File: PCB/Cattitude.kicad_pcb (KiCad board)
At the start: 2 copper layers, 35 x 25 mm, 14 parts, among them J1 Conn_01x08_Pin, J2 Conn_01x04_Pin, J3 Conn_01x02_Pin, J4 Conn_01x02_Pin, J5 Conn_01x03_Pin, J6 Conn_01x03_Pin, J7 Conn_01x03_Pin, J8 Conn_01x03_Pin, SW2 SW_SPDT, U1 102010551

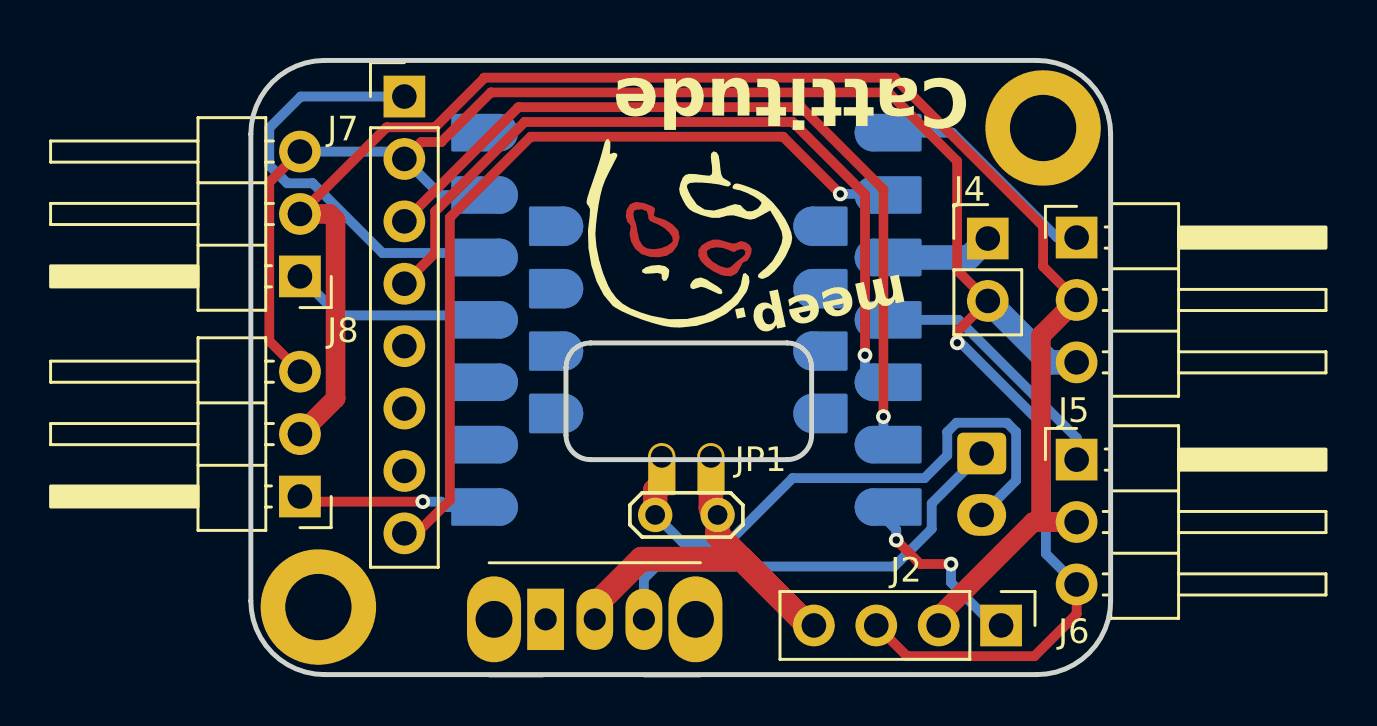
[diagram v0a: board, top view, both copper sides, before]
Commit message: Added GND Pour
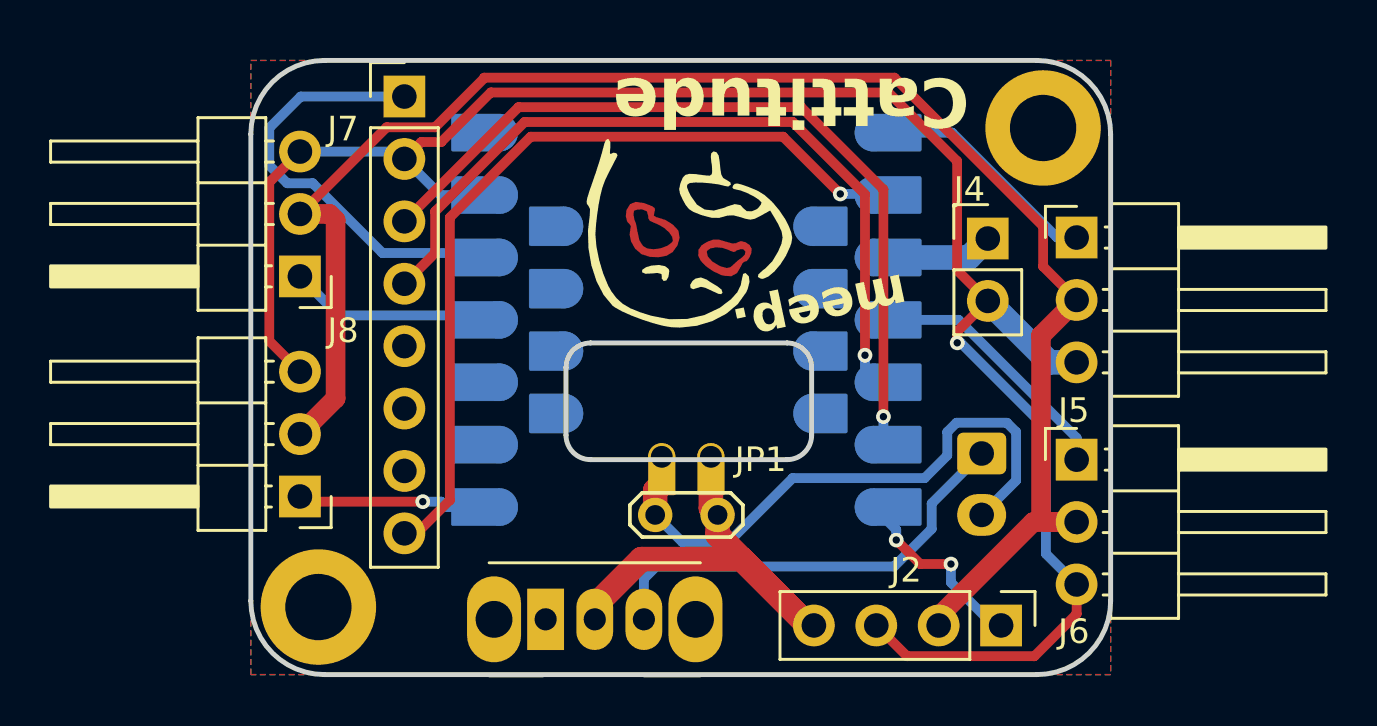
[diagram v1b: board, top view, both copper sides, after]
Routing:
- added copper zone on B.Cu, net GND
- added copper zone on F.Cu, net GND
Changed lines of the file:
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@@
 		(net 28)
+	)
+	(zone
+		(net 3)
+		(net_name "GND")
+		(layers "F.Cu" "B.Cu")
+		(hatch edge 0.5)
+		(connect_pads
+			(clearance 0.5)
+		)
+		(min_thickness 0.25)
+		(filled_areas_thickness no)
+		(fill yes
+			(thermal_gap 0.5)
+			(thermal_bridge_width 0.5)
+		)
+		(polygon
+			(pts
+				(xy 25 50) (xy 25 25) (xy 60 25) (xy 60 50)
+			)
+		)
 	)
 	(embedded_fonts no)
